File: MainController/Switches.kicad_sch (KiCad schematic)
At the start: 0 parts

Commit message: WIP likely need to switch 12V signalling around
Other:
- note added: "TODO Forward, Reverse. Neutral Implicit."
- note added: "TODO key switch - 2 positions"
- note removed: "TODO Foward/Reverse/Neutral Switch"
- note removed: "TODO key switch"
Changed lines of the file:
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@@
 	(generator_version "8.0")
 	(paper "A4")
-	(text "TODO Foward/Reverse/Neutral Switch"
+	(text "TODO Forward, Reverse. Neutral Implicit."
 		(exclude_from_sim no)
-		(at 42.418 49.784 0)
+		(at 36.322 49.784 0)
 		(effects
 			(font
@@
 	(text "TODO Brake Pedal Switch"
 		(exclude_from_sim no)
-		(at 43.942 43.434 0)
+		(at 36.83 45.72 0)
 		(effects
 			(font
@@
 	(text "TODO light switch"
 		(exclude_from_sim no)
-		(at 42.926 36.83 0)
+		(at 36.83 41.91 0)
 		(effects
 			(font
@@
 		)
 	)
-	(text "TODO key switch"
+	(text "TODO key switch - 2  positions"
 		(exclude_from_sim no)
-		(at 42.672 29.464 0)
+		(at 36.322 38.354 0)
 		(effects
 			(font
@@
 	(text "TODO Horn?"
 		(exclude_from_sim no)
-		(at 43.18 57.658 0)
+		(at 36.322 58.166 0)
 		(effects
 			(font
@@
 	(text "TODO Hand Brake?"
 		(exclude_from_sim no)
-		(at 43.18 53.848 0)
+		(at 35.814 54.102 0)
 		(effects
 			(font
@@
 	(text "TODO Brights"
 		(exclude_from_sim no)
-		(at 42.164 77.216 0)
+		(at 35.814 86.106 0)
 		(effects
 			(font
@@
 	(text "TODO SSRs?"
 		(exclude_from_sim no)
-		(at 95.25 55.626 90)
+		(at 88.9 64.516 90)
 		(effects
 			(font
@@
 	(text "TODO Turn Signal Left\nTODO Turn Signal Right"
 		(exclude_from_sim no)
-		(at 42.418 65.786 0)
+		(at 36.068 74.676 0)
 		(effects
 			(font
@@
 		)
 	)
+	(label "12V_IN_+"
+		(at 22.86 15.24 0)
+		(effects
+			(font
+				(size 1.27 1.27)
+			)
+			(justify left bottom)
+		)
+	)
+	(hierarchical_label "12V_IN_+"
+		(shape input)
+		(at 22.86 15.24 180)
+		(effects
+			(font
+				(size 1.27 1.27)
+			)
+			(justify right)
+		)
+	)

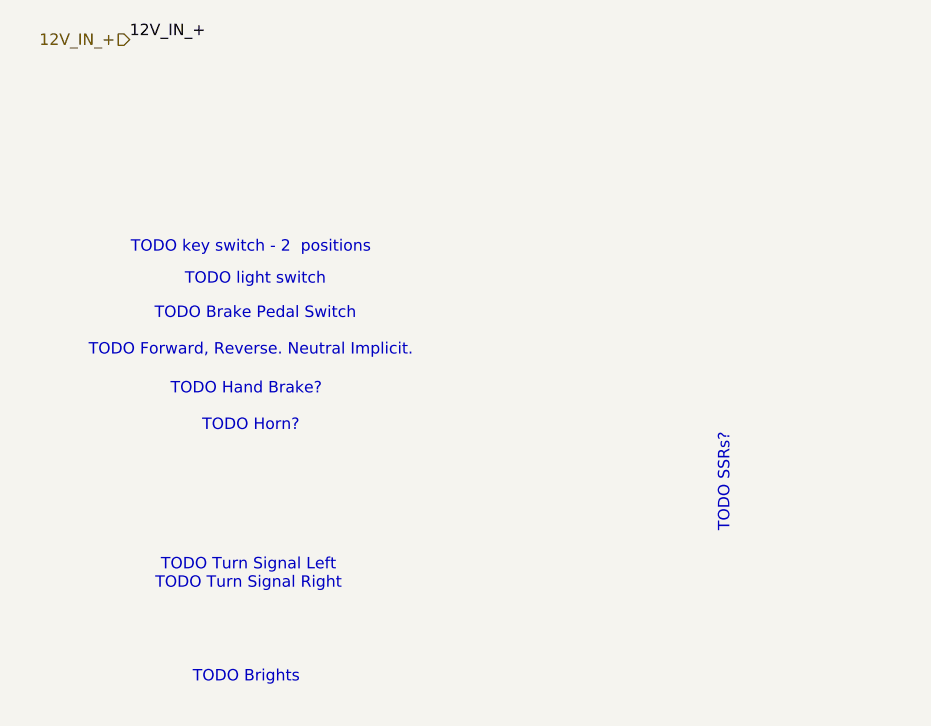
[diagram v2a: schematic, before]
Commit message: Adding Labels for Switches
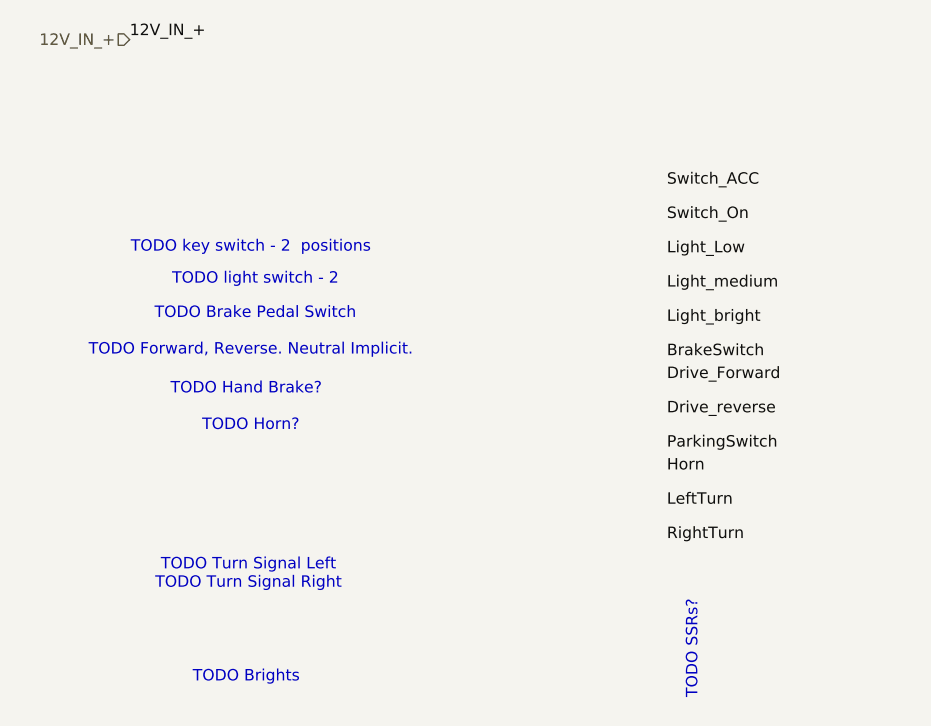
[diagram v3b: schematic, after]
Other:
- note added: "TODO light switch - 2"
- note removed: "TODO light switch"
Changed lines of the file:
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@@
 		)
 	)
-	(text "TODO light switch"
+	(text "TODO light switch - 2"
 		(exclude_from_sim no)
 		(at 36.83 41.91 0)
@@
 	(text "TODO SSRs?"
 		(exclude_from_sim no)
-		(at 88.9 64.516 90)
+		(at 85.344 83.058 90)
 		(effects
 			(font
@@
 		)
 	)
+	(label "Drive_Forward"
+		(at 82.55 53.34 0)
+		(effects
+			(font
+				(size 1.27 1.27)
+			)
+			(justify left bottom)
+		)
+	)
+	(label "Switch_On"
+		(at 82.55 35.56 0)
+		(effects
+			(font
+				(size 1.27 1.27)
+			)
+			(justify left bottom)
+		)
+	)
+	(label "Drive_reverse"
+		(at 82.55 57.15 0)
+		(effects
+			(font
+				(size 1.27 1.27)
+			)
+			(justify left bottom)
+		)
+	)
+	(label "BrakeSwitch"
+		(at 82.55 50.8 0)
+		(effects
+			(font
+				(size 1.27 1.27)
+			)
+			(justify left bottom)
+		)
+	)
+	(label "Horn"
+		(at 82.55 63.5 0)
+		(effects
+			(font
+				(size 1.27 1.27)
+			)
+			(justify left bottom)
+		)
+	)
+	(label "Switch_ACC"
+		(at 82.55 31.75 0)
+		(effects
+			(font
+				(size 1.27 1.27)
+			)
+			(justify left bottom)
+		)
+	)
+	(label "Light_Low"
+		(at 82.55 39.37 0)
+		(effects
+			(font
+				(size 1.27 1.27)
+			)
+			(justify left bottom)
+		)
+	)
+	(label "Light_medium"
+		(at 82.55 43.18 0)
+		(effects
+			(font
+				(size 1.27 1.27)
+			)
+			(justify left bottom)
+		)
+	)
+	(label "LeftTurn"
+		(at 82.55 67.31 0)
+		(effects
+			(font
+				(size 1.27 1.27)
+			)
+			(justify left bottom)
+		)
+	)
+	(label "RightTurn"
+		(at 82.55 71.12 0)
+		(effects
+			(font
+				(size 1.27 1.27)
+			)
+			(justify left bottom)
+		)
+	)
+	(label "ParkingSwitch"
+		(at 82.55 60.96 0)
+		(effects
+			(font
+				(size 1.27 1.27)
+			)
+			(justify left bottom)
+		)
+	)
 	(label "12V_IN_+"
 		(at 22.86 15.24 0)
 		(effects
 			(font
+				(size 1.27 1.27)
+			)
+			(justify left bottom)
+		)
+	)
+	(label "Light_bright"
+		(at 82.55 46.99 0)
+		(effects
+			(font

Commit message: Added Polyfuse
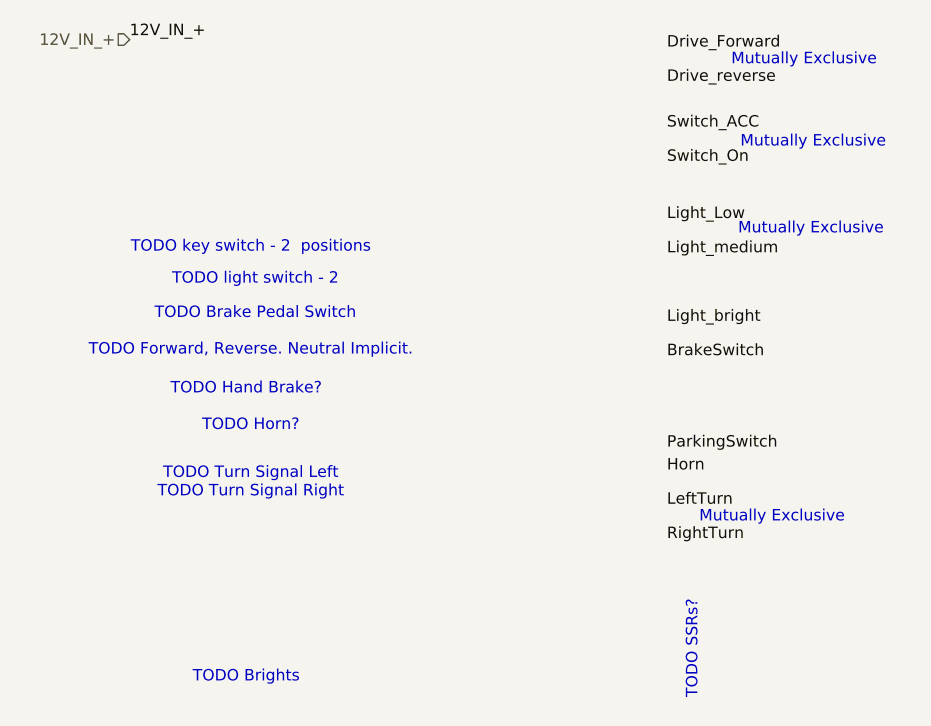
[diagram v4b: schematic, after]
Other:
- note added: "Mutually Exclusive"
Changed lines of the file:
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@@
 	(generator_version "8.0")
 	(paper "A4")
+	(text "Mutually Exclusive"
+		(exclude_from_sim no)
+		(at 94.234 68.326 0)
+		(effects
+			(font
+				(size 1.27 1.27)
+			)
+		)
+	)
 	(text "TODO Forward, Reverse. Neutral Implicit."
 		(exclude_from_sim no)
@@
 		(exclude_from_sim no)
 		(at 36.83 45.72 0)
+		(effects
+			(font
+				(size 1.27 1.27)
+			)
+		)
+	)
+	(text "Mutually Exclusive"
+		(exclude_from_sim no)
+		(at 97.79 17.526 0)
 		(effects
 			(font
@@
 		)
 	)
+	(text "Mutually Exclusive"
+		(exclude_from_sim no)
+		(at 98.806 26.67 0)
+		(effects
+			(font
+				(size 1.27 1.27)
+			)
+		)
+	)
+	(text "Mutually Exclusive"
+		(exclude_from_sim no)
+		(at 98.552 36.322 0)
+		(effects
+			(font
+				(size 1.27 1.27)
+			)
+		)
+	)
 	(text "TODO Brights"
 		(exclude_from_sim no)
@@
 	(text "TODO Turn Signal Left\nTODO Turn Signal Right"
 		(exclude_from_sim no)
-		(at 36.068 74.676 0)
+		(at 36.322 64.516 0)
 		(effects
 			(font
@@
 	)
 	(label "Drive_Forward"
-		(at 82.55 53.34 0)
+		(at 82.55 16.51 0)
 		(effects
 			(font
@@
 	)
 	(label "Switch_On"
-		(at 82.55 35.56 0)
+		(at 82.55 29.21 0)
 		(effects
 			(font
@@
 	)
 	(label "Drive_reverse"
-		(at 82.55 57.15 0)
+		(at 82.55 20.32 0)
 		(effects
 			(font
@@
 	)
 	(label "Switch_ACC"
-		(at 82.55 31.75 0)
+		(at 82.55 25.4 0)
 		(effects
 			(font
@@
 	)
 	(label "Light_Low"
-		(at 82.55 39.37 0)
+		(at 82.55 35.56 0)
 		(effects
 			(font
@@
 	)
 	(label "Light_medium"
-		(at 82.55 43.18 0)
+		(at 82.55 39.37 0)
 		(effects
 			(font
